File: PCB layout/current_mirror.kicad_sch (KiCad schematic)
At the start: 21 parts, among them J1 12V INPUT, Q1 2N3904, Q2 2N3904

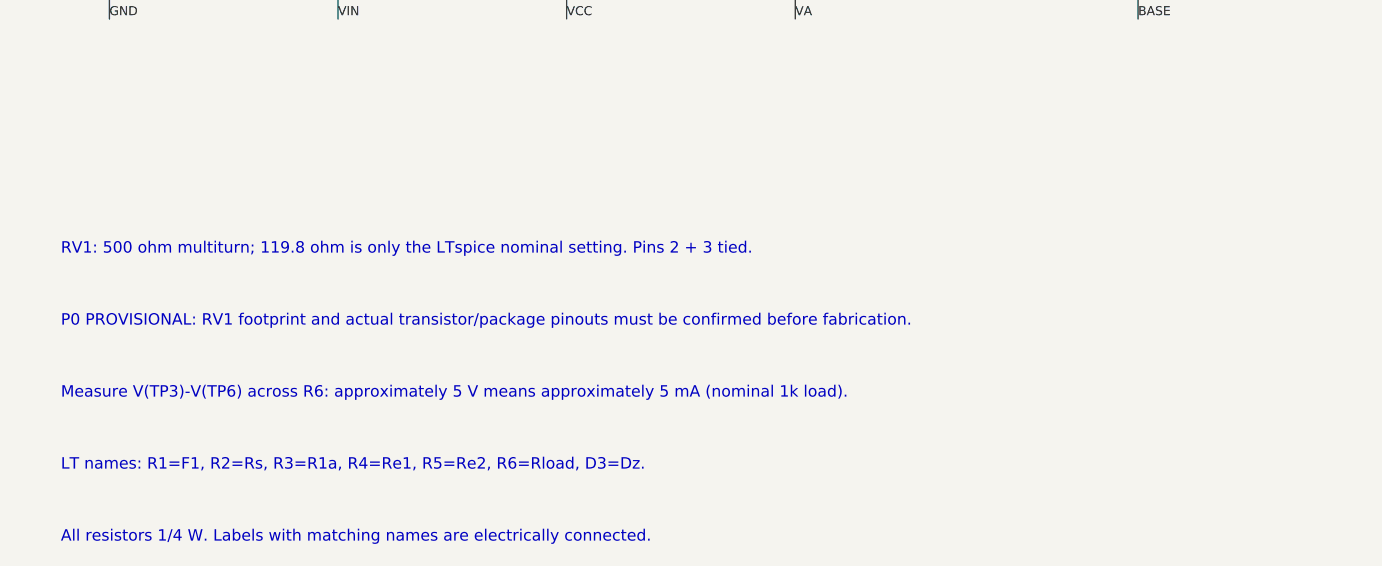
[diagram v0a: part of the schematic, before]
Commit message: Fit measured trimmer geometry and retain unverified pinout status
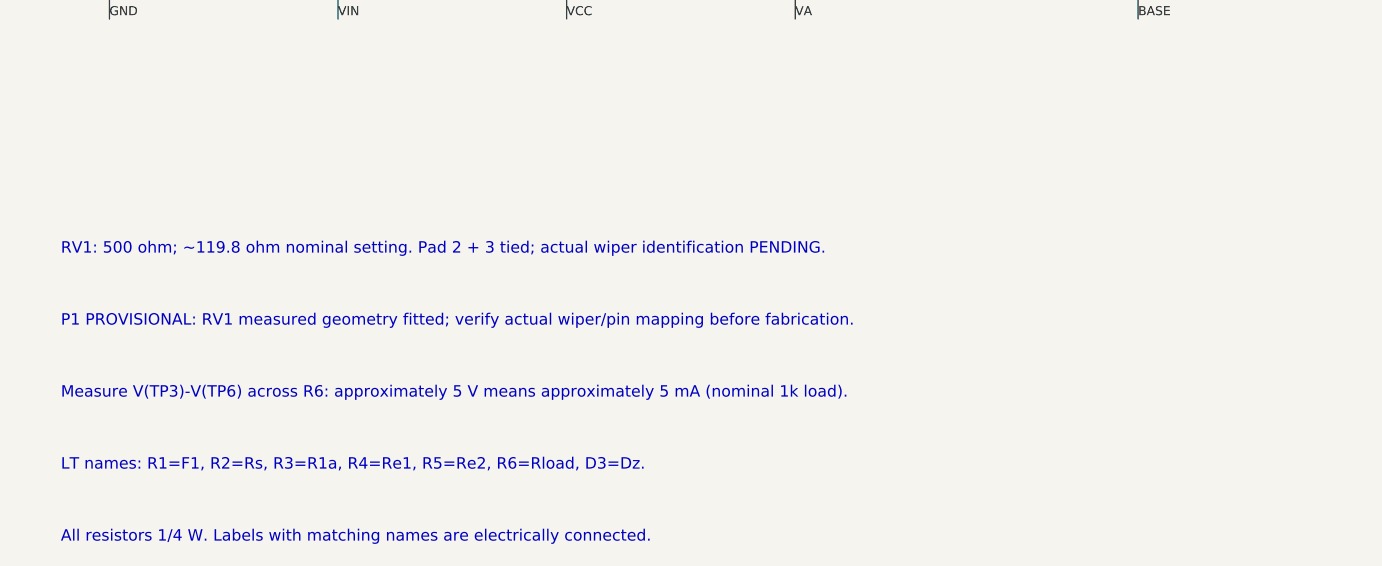
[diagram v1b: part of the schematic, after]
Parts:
- RV1: footprint Project:RV1_PENDING -> Project:RV1_D9_P8_Offset5_PINOUT_UNVERIFIED
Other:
- note added: "P1 PROVISIONAL: RV1 measured geometry fitted; verify actual wiper/pin mapping before fabrication."
- note added: "RV1: 500 ohm; ~119.8 ohm nominal setting. Pad 2 + 3 tied; actual wiper identification PENDING."
- note removed: "P0 PROVISIONAL: RV1 footprint and actual transistor/package pinouts must be confirmed before fabrication."
- note removed: "RV1: 500 ohm multiturn; 119.8 ohm is only the LTspice nominal setting. Pins 2 + 3 tied."
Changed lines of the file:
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@@
 (kicad_sch (version 20250114) (generator "pcb_layout_script") (paper "A4")
-(title_block (title "5 mA diode-compensated current mirror") (rev "P0 - TRIMMER FOOTPRINT PENDING") (comment 1 "Exact LTspice connectivity; added power connector and voltage test points"))
+(title_block (title "5 mA diode-compensated current mirror") (rev "P1 - VERIFY RV1 WIPER") (comment 1 "Exact LTspice connectivity; added power connector and voltage test points"))
 (symbol (lib_id "Connector_Generic:Conn_01x02") (at 25.4 40.64 0) (unit 1) (in_bom yes) (on_board yes) (dnp no)
 (property "Reference" "J1" (at 30.479999999999997 35.56 0) (effects (font (size 1.0 1.0)) (justify left) ))
@@
 (property "Reference" "RV1" (at 144.78 71.12 0) (effects (font (size 1.0 1.0)) (justify left) ))
 (property "Value" "500R TRIM / set ~119.8R" (at 144.78 73.66 0) (effects (font (size 1.0 1.0)) (justify left) ))
-(property "Footprint" "Project:RV1_PENDING" (at 139.7 76.2 0) (effects (font (size 1.0 1.0)) (justify left) (hide yes)))
+(property "Footprint" "Project:RV1_D9_P8_Offset5_PINOUT_UNVERIFIED" (at 139.7 76.2 0) (effects (font (size 1.0 1.0)) (justify left) (hide yes)))
 (pin "1")
 (pin "2")
@@
 (label "OUT" (at 177.8 119.38 0) (effects (font (size 1.0 1.0)) (justify left bottom)))
 (text "SUPPLY: J1 -> R1 -> D4 -> VCC. R1 is a resistor, not a fuse." (at 20 20 0) (effects (font (size 1.27 1.27)) (justify left)))
-(text "RV1: 500 ohm multiturn; 119.8 ohm is only the LTspice nominal setting. Pins 2 + 3 tied." (at 20 145 0) (effects (font (size 1.27 1.27)) (justify left)))
-(text "P0 PROVISIONAL: RV1 footprint and actual transistor/package pinouts must be confirmed before fabrication." (at 20 153 0) (effects (font (size 1.27 1.27)) (justify left)))
+(text "RV1: 500 ohm; ~119.8 ohm nominal setting. Pad 2 + 3 tied; actual wiper identification PENDING." (at 20 145 0) (effects (font (size 1.27 1.27)) (justify left)))
+(text "P1 PROVISIONAL: RV1 measured geometry fitted; verify actual wiper/pin mapping before fabrication." (at 20 153 0) (effects (font (size 1.27 1.27)) (justify left)))
 (text "Measure V(TP3)-V(TP6) across R6: approximately 5 V means approximately 5 mA (nominal 1k load)." (at 20 161 0) (effects (font (size 1.27 1.27)) (justify left)))
 (text "LT names: R1=F1, R2=Rs, R3=R1a, R4=Re1, R5=Re2, R6=Rload, D3=Dz." (at 20 169 0) (effects (font (size 1.27 1.27)) (justify left)))

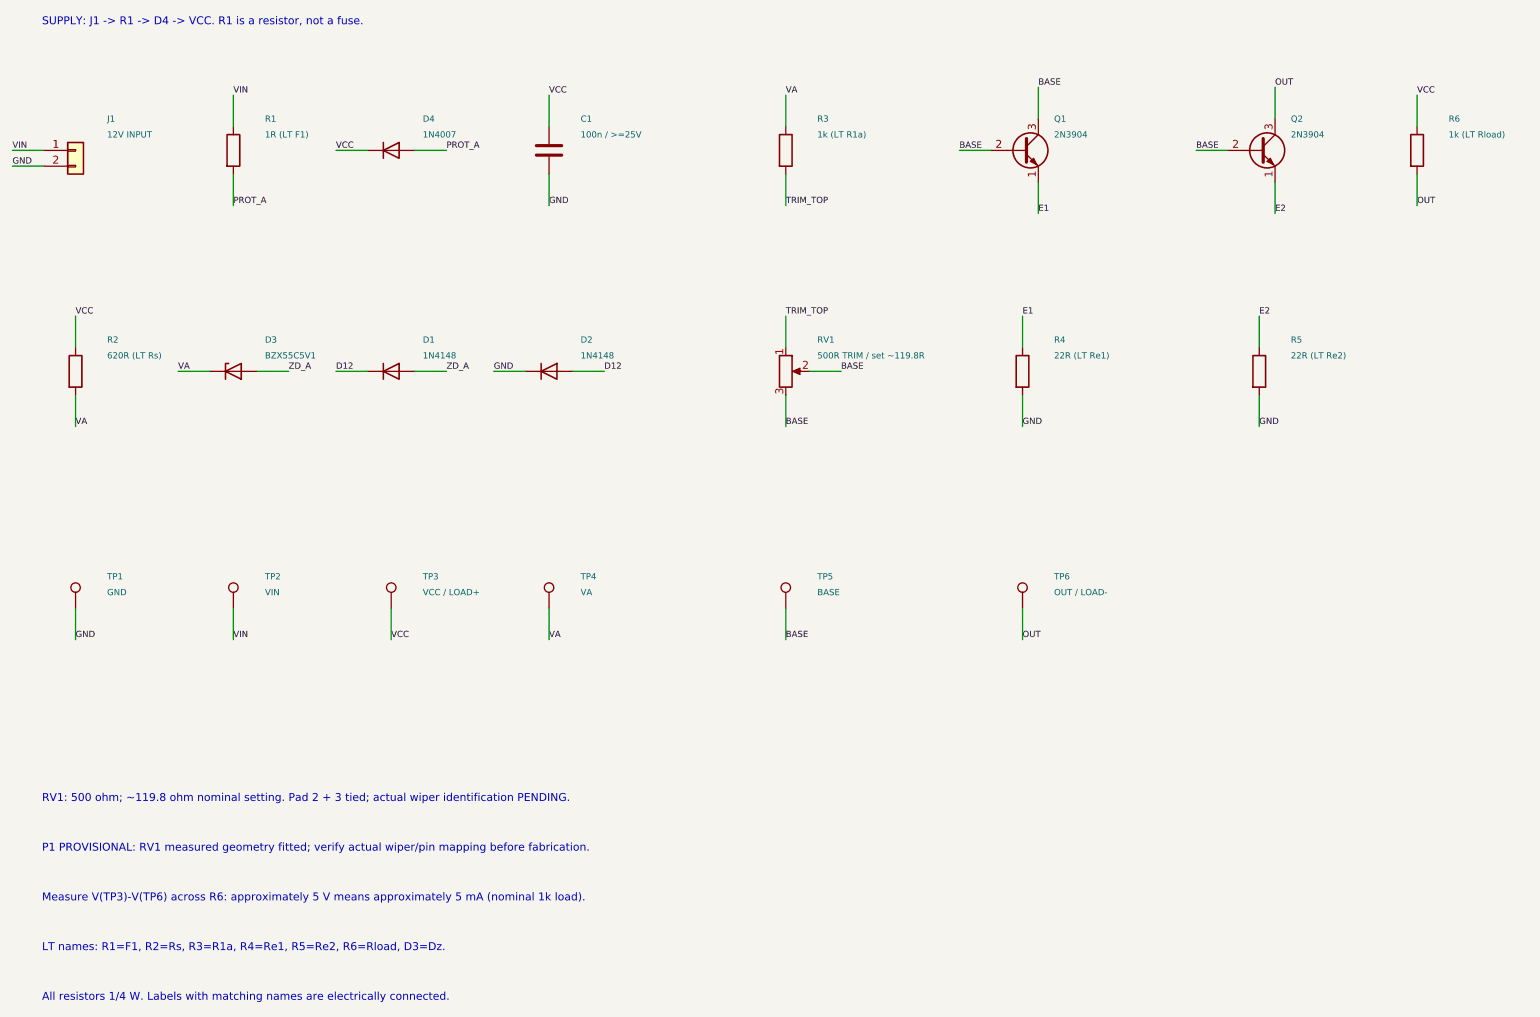
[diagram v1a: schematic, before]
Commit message: Replace trimmer with fixed 120 ohm resistor and validate P2 PCB
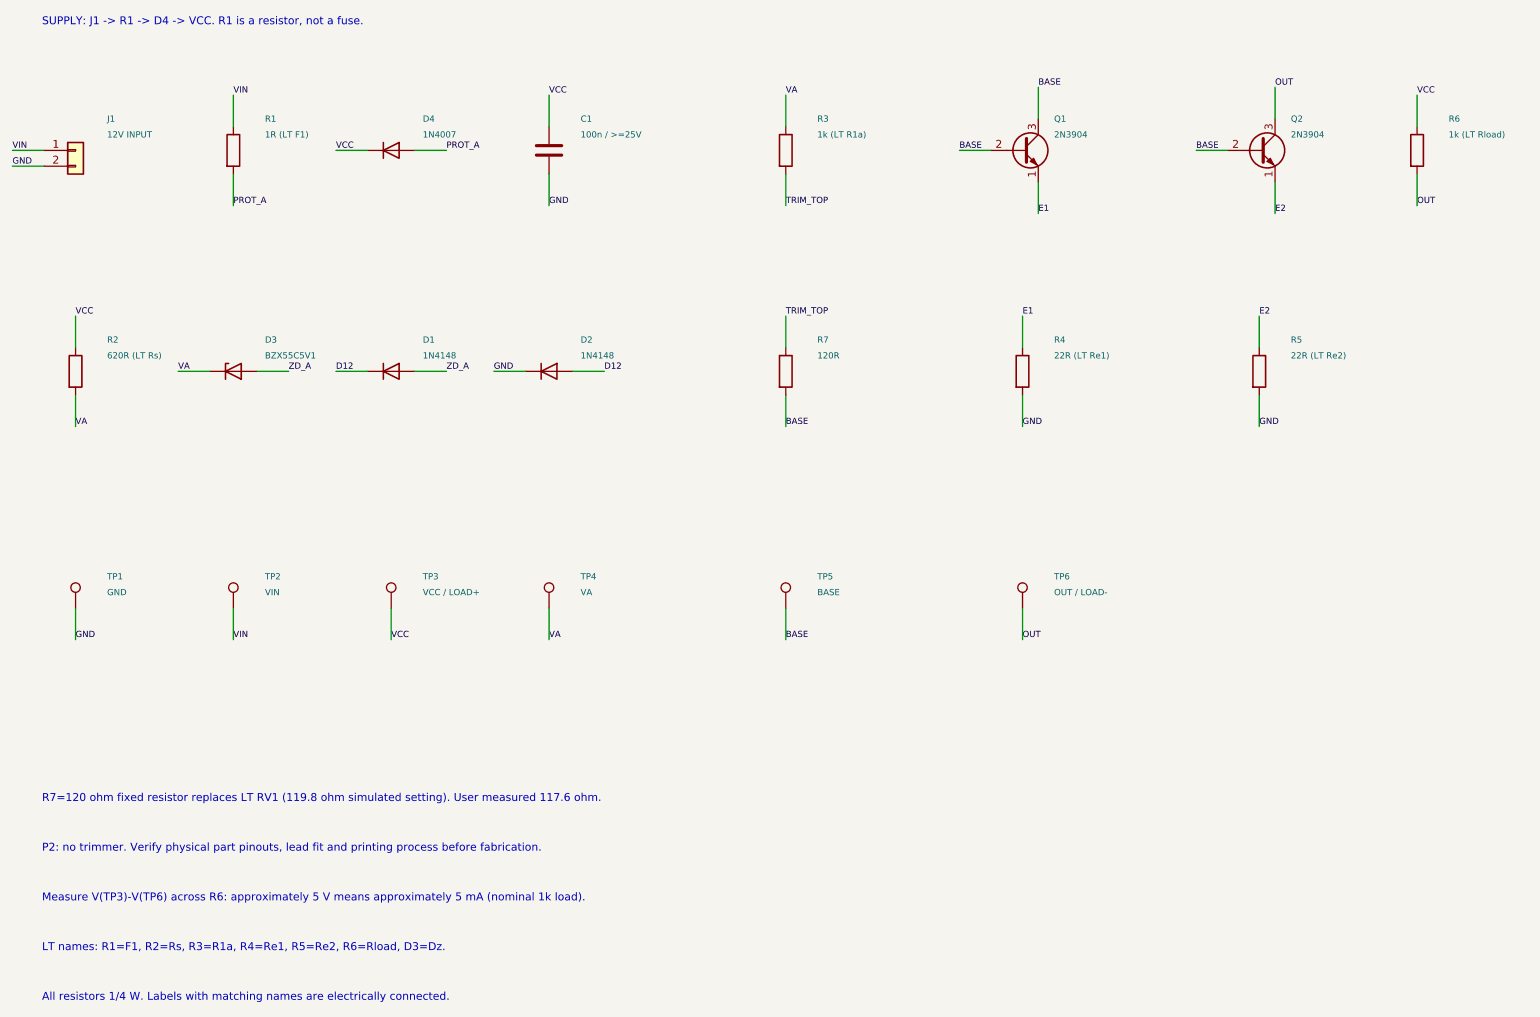
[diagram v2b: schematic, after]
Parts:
- removed RV1: 500R TRIM / set ~119.8R, Project:RV1_D9_P8_Offset5_PINOUT_UNVERIFIED, symbol Device:R_Potentiometer
- added R7: 120R, Project:R7_ETCH, symbol Device:R
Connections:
- net BASE: now also R7.2
- net TRIM_TOP: now also R7.1
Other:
- note added: "P2: no trimmer. Verify physical part pinouts, lead fit and printing process before fabrication."
- note added: "R7=120 ohm fixed resistor replaces LT RV1 (119.8 ohm simulated setting). User measured 117.6 ohm."
- note removed: "P1 PROVISIONAL: RV1 measured geometry fitted; verify actual wiper/pin mapping before fabrication."
- note removed: "RV1: 500 ohm; ~119.8 ohm nominal setting. Pad 2 + 3 tied; actual wiper identification PENDING."
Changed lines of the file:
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@@
 (kicad_sch (version 20250114) (generator "pcb_layout_script") (paper "A4")
-(title_block (title "5 mA diode-compensated current mirror") (rev "P1 - VERIFY RV1 WIPER") (comment 1 "Exact LTspice connectivity; added power connector and voltage test points"))
+(title_block (title "5 mA diode-compensated current mirror") (rev "P2 - FIXED 120R") (comment 1 "LTspice topology; RV1 replaced by fixed R7=120R at user request"))
 (symbol (lib_id "Connector_Generic:Conn_01x02") (at 25.4 40.64 0) (unit 1) (in_bom yes) (on_board yes) (dnp no)
 (property "Reference" "J1" (at 30.479999999999997 35.56 0) (effects (font (size 1.0 1.0)) (justify left) ))
@@
 (wire (pts (xy 139.7 44.45) (xy 139.7 49.53)) (stroke (width 0) (type default)))
 (label "TRIM_TOP" (at 139.7 49.53 0) (effects (font (size 1.0 1.0)) (justify left bottom)))
-(symbol (lib_id "Device:R_Potentiometer") (at 139.7 76.2 0) (unit 1) (in_bom yes) (on_board yes) (dnp no)
-(property "Reference" "RV1" (at 144.78 71.12 0) (effects (font (size 1.0 1.0)) (justify left) ))
-(property "Value" "500R TRIM / set ~119.8R" (at 144.78 73.66 0) (effects (font (size 1.0 1.0)) (justify left) ))
-(property "Footprint" "Project:RV1_D9_P8_Offset5_PINOUT_UNVERIFIED" (at 139.7 76.2 0) (effects (font (size 1.0 1.0)) (justify left) (hide yes)))
-(pin "1")
-(pin "2")
-(pin "3")
-(instances (project "current_mirror" (path "/9e16e4a6-c072-58dd-bcd3-75d7d6cad8fa" (reference "RV1") (unit 1)))))
+(symbol (lib_id "Device:R") (at 139.7 76.2 0) (unit 1) (in_bom yes) (on_board yes) (dnp no)
+(property "Reference" "R7" (at 144.78 71.12 0) (effects (font (size 1.0 1.0)) (justify left) ))
+(property "Value" "120R" (at 144.78 73.66 0) (effects (font (size 1.0 1.0)) (justify left) ))
+(property "Footprint" "Project:R7_ETCH" (at 139.7 76.2 0) (effects (font (size 1.0 1.0)) (justify left) (hide yes)))
+(pin "1")
+(pin "2")
+(instances (project "current_mirror" (path "/9e16e4a6-c072-58dd-bcd3-75d7d6cad8fa" (reference "R7") (unit 1)))))
 (wire (pts (xy 139.7 72.39) (xy 139.7 67.31)) (stroke (width 0) (type default)))
 (label "TRIM_TOP" (at 139.7 67.31 0) (effects (font (size 1.0 1.0)) (justify left bottom)))
-(wire (pts (xy 143.51 76.2) (xy 148.59 76.2)) (stroke (width 0) (type default)))
-(label "BASE" (at 148.59 76.2 0) (effects (font (size 1.0 1.0)) (justify left bottom)))
 (wire (pts (xy 139.7 80.01) (xy 139.7 85.09)) (stroke (width 0) (type default)))
 (label "BASE" (at 139.7 85.09 0) (effects (font (size 1.0 1.0)) (justify left bottom)))
@@
 (label "OUT" (at 177.8 119.38 0) (effects (font (size 1.0 1.0)) (justify left bottom)))
 (text "SUPPLY: J1 -> R1 -> D4 -> VCC. R1 is a resistor, not a fuse." (at 20 20 0) (effects (font (size 1.27 1.27)) (justify left)))
-(text "RV1: 500 ohm; ~119.8 ohm nominal setting. Pad 2 + 3 tied; actual wiper identification PENDING." (at 20 145 0) (effects (font (size 1.27 1.27)) (justify left)))
-(text "P1 PROVISIONAL: RV1 measured geometry fitted; verify actual wiper/pin mapping before fabrication." (at 20 153 0) (effects (font (size 1.27 1.27)) (justify left)))
+(text "R7=120 ohm fixed resistor replaces LT RV1 (119.8 ohm simulated setting). User measured 117.6 ohm." (at 20 145 0) (effects (font (size 1.27 1.27)) (justify left)))
+(text "P2: no trimmer. Verify physical part pinouts, lead fit and printing process before fabrication." (at 20 153 0) (effects (font (size 1.27 1.27)) (justify left)))
 (text "Measure V(TP3)-V(TP6) across R6: approximately 5 V means approximately 5 mA (nominal 1k load)." (at 20 161 0) (effects (font (size 1.27 1.27)) (justify left)))
 (text "LT names: R1=F1, R2=Rs, R3=R1a, R4=Re1, R5=Re2, R6=Rload, D3=Dz." (at 20 169 0) (effects (font (size 1.27 1.27)) (justify left)))
